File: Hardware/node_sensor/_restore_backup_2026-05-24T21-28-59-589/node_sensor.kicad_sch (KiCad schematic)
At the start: 14 parts, among them J1 Conn_Jack-DC, J2 Pump, J3 Light, U1 DevKitESP32, U2 DHT11, U3 BH1750, U4 ADS1115, U5 DS3231, U6 Soil-Moisture, U7 Soil-Moisture, U8 Soil-Moisture, U9 Soil-Moisture

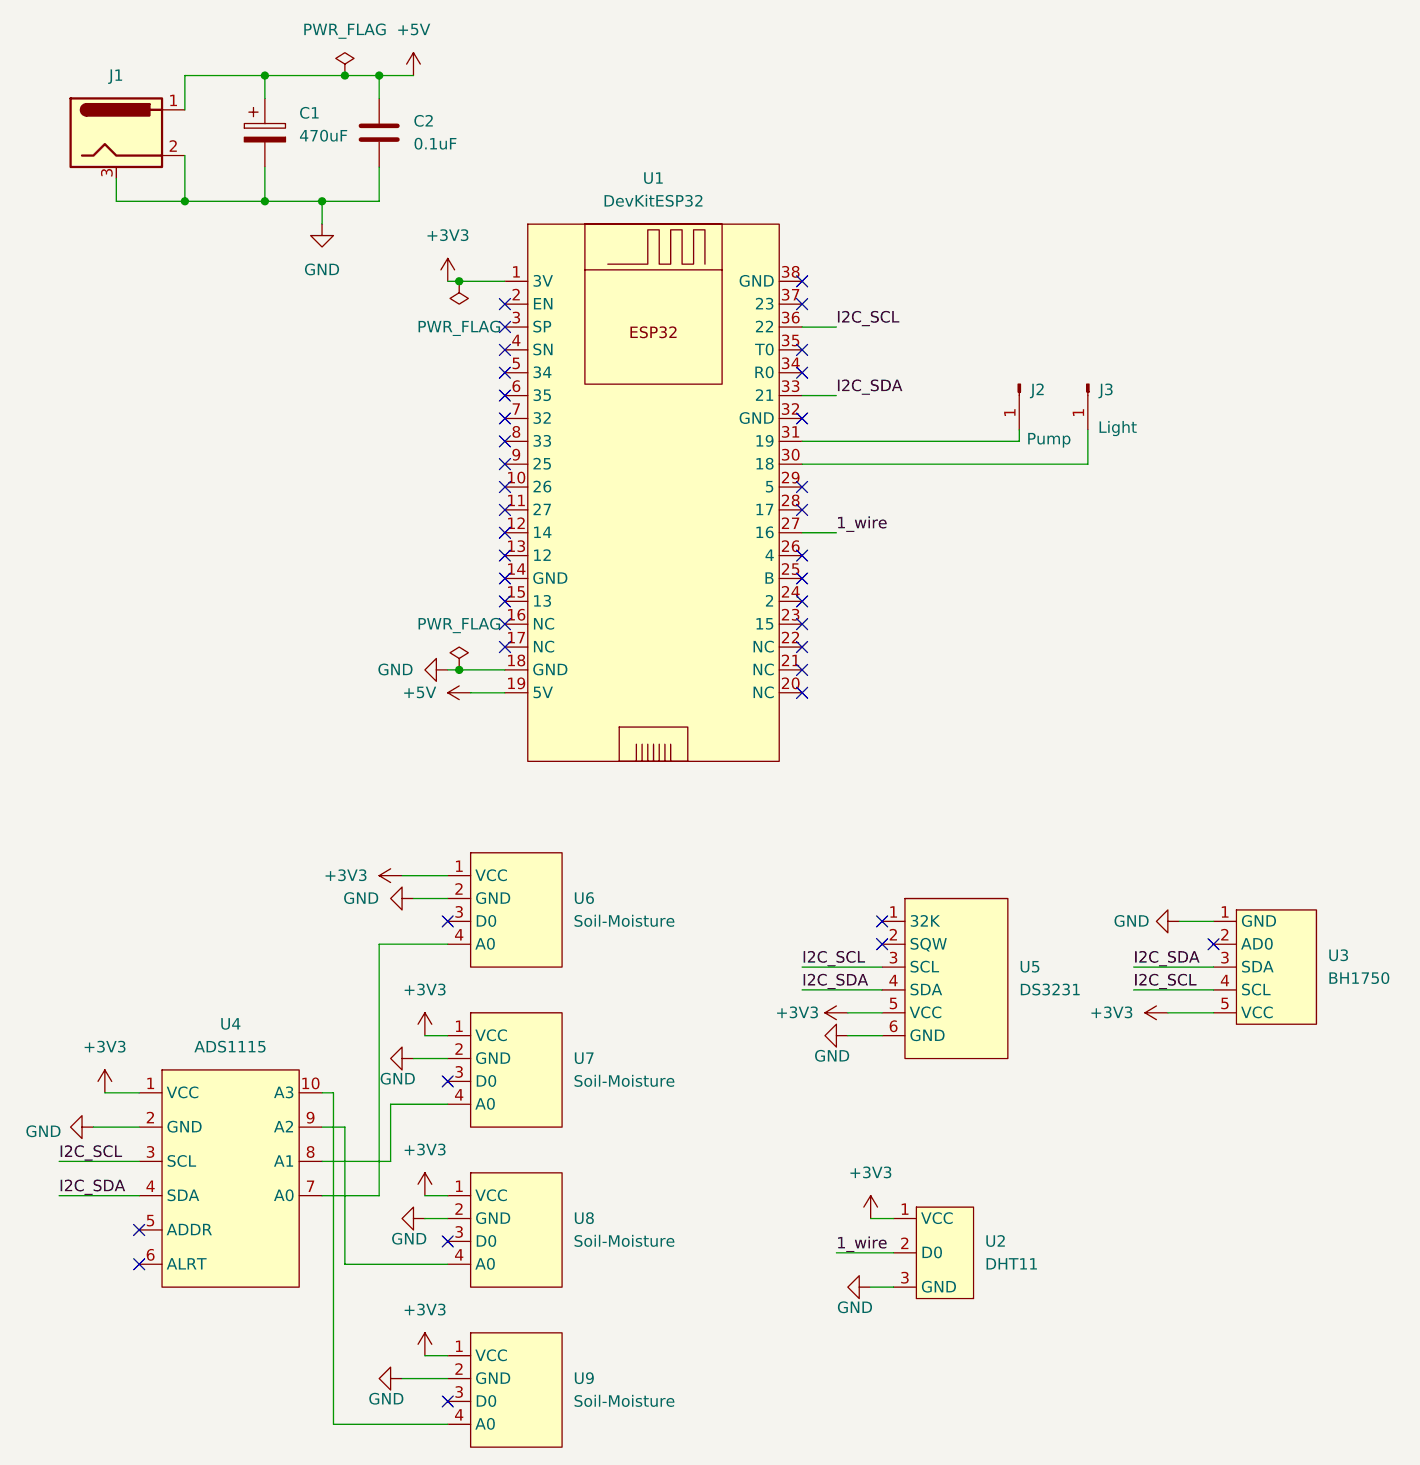
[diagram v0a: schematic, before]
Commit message: updated hardware + fixed conflict Gatway
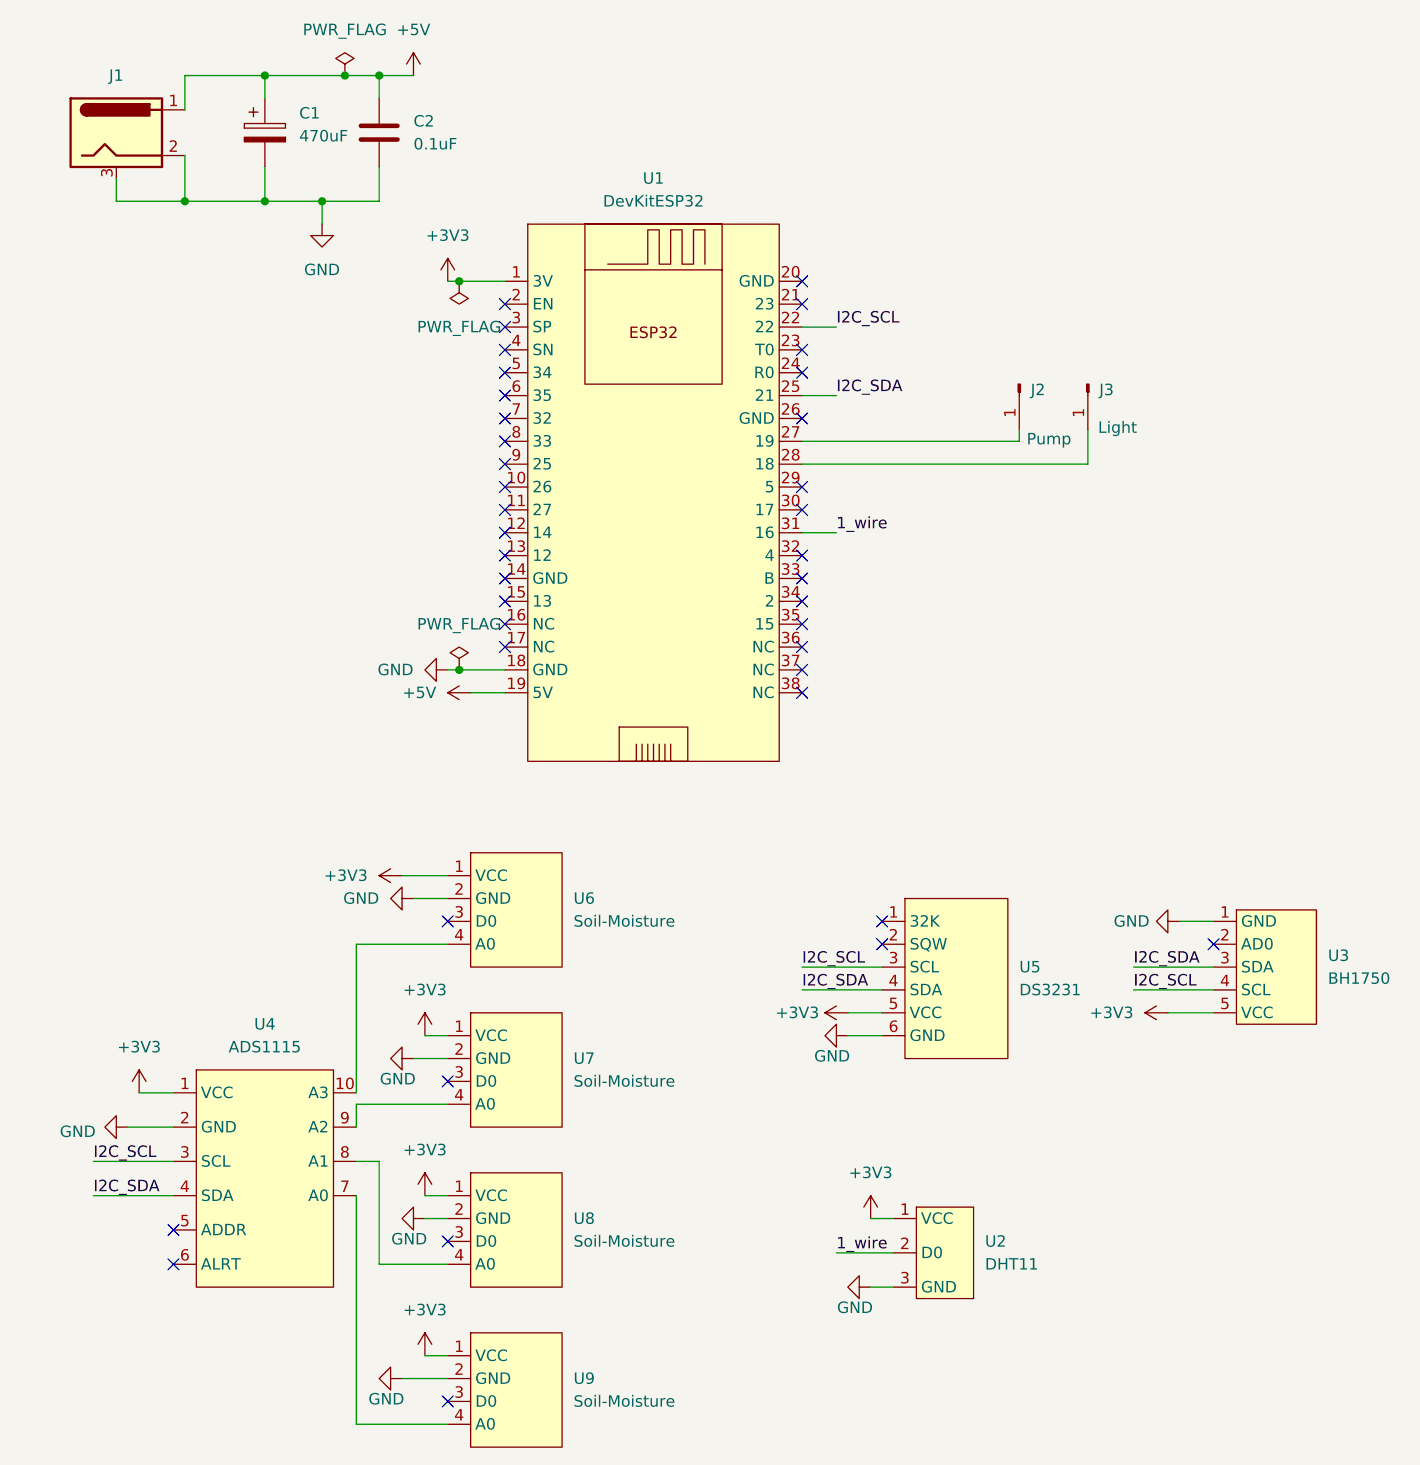
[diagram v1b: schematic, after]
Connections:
- net 1_wire: now also U1.31 (16); no longer U1.27 (16)
- net I2C_SCL: now also U1.22; no longer U1.36 (22)
- net I2C_SDA: now also U1.25 (21); no longer U1.33 (21)
- net at U4.10 (A3): now also U6.4 (A0); no longer U9.4 (A0)
- net at U4.7 (A0): now also U9.4 (A0); no longer U6.4 (A0)
- net at U4.8 (A1): now also U8.4 (A0); no longer U7.4 (A0)
- net at U4.9 (A2): now also U7.4 (A0); no longer U8.4 (A0)
- net at U1.28 (18): now also J3.1 (Pin_1)
- net at U1.30 (17): no longer J3.1 (Pin_1)
- net at J2.1 (Pin_1): now also U1.27 (19); no longer U1.31 (19)
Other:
- moved on the sheet: U4
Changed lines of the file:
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@@
 	)
 	(no_connect
-		(at 25.4 148.59)
+		(at 29.21 148.59)
 	)
 	(no_connect
@@
 	)
 	(no_connect
-		(at 25.4 152.4)
+		(at 29.21 152.4)
 	)
 	(wire
 		(pts
-			(xy 22.86 34.29) (xy 30.48 34.29)
+			(xy 52.07 140.97) (xy 52.07 152.4)
 		)
 		(stroke
@@
 	(wire
 		(pts
-			(xy 59.69 86.36) (xy 60.96 86.36)
+			(xy 22.86 34.29) (xy 30.48 34.29)
 		)
 		(stroke
@@
 	(wire
 		(pts
-			(xy 16.51 144.78) (xy 25.4 144.78)
+			(xy 59.69 86.36) (xy 60.96 86.36)
 		)
 		(stroke
@@
 	(wire
 		(pts
-			(xy 30.48 34.29) (xy 39.37 34.29)
+			(xy 20.32 144.78) (xy 29.21 144.78)
 		)
 		(stroke
@@
 	(wire
 		(pts
-			(xy 54.61 109.22) (xy 59.69 109.22)
+			(xy 30.48 34.29) (xy 39.37 34.29)
 		)
 		(stroke
@@
 	(wire
 		(pts
-			(xy 59.69 43.18) (xy 60.96 43.18)
+			(xy 54.61 109.22) (xy 59.69 109.22)
 		)
 		(stroke
@@
 	(wire
 		(pts
-			(xy 99.06 71.12) (xy 102.87 71.12)
+			(xy 59.69 43.18) (xy 60.96 43.18)
 		)
 		(stroke
@@
 	(wire
 		(pts
-			(xy 60.96 86.36) (xy 66.04 86.36)
+			(xy 99.06 71.12) (xy 102.87 71.12)
 		)
 		(stroke
@@
 	(wire
 		(pts
-			(xy 60.96 43.18) (xy 66.04 43.18)
+			(xy 49.53 137.16) (xy 49.53 134.62)
 		)
 		(stroke
@@
 	(wire
 		(pts
-			(xy 99.06 119.38) (xy 107.95 119.38)
+			(xy 60.96 86.36) (xy 66.04 86.36)
 		)
 		(stroke
@@
 	(wire
 		(pts
-			(xy 48.26 20.32) (xy 52.07 20.32)
+			(xy 49.53 134.62) (xy 59.69 134.62)
 		)
 		(stroke
@@
 	(wire
 		(pts
-			(xy 21.59 133.35) (xy 25.4 133.35)
+			(xy 60.96 43.18) (xy 66.04 43.18)
 		)
 		(stroke
@@
 	(wire
 		(pts
-			(xy 99.06 60.96) (xy 123.19 60.96)
+			(xy 99.06 119.38) (xy 107.95 119.38)
 		)
 		(stroke
@@
 	(wire
 		(pts
-			(xy 57.15 162.56) (xy 59.69 162.56)
+			(xy 48.26 20.32) (xy 52.07 20.32)
 		)
 		(stroke
@@
 	(wire
 		(pts
-			(xy 22.86 31.75) (xy 22.86 34.29)
+			(xy 49.53 133.35) (xy 49.53 116.84)
 		)
 		(stroke
@@
 	(wire
 		(pts
-			(xy 52.07 20.32) (xy 52.07 22.86)
+			(xy 25.4 133.35) (xy 29.21 133.35)
 		)
 		(stroke
@@
 	(wire
 		(pts
-			(xy 59.69 116.84) (xy 52.07 116.84)
+			(xy 99.06 60.96) (xy 123.19 60.96)
 		)
 		(stroke
@@
 	(wire
 		(pts
-			(xy 53.34 140.97) (xy 45.72 140.97)
+			(xy 57.15 162.56) (xy 59.69 162.56)
 		)
 		(stroke
@@
 	(wire
 		(pts
-			(xy 39.37 20.32) (xy 48.26 20.32)
+			(xy 22.86 31.75) (xy 22.86 34.29)
 		)
 		(stroke
@@
 	(wire
 		(pts
-			(xy 53.34 134.62) (xy 53.34 140.97)
+			(xy 52.07 20.32) (xy 52.07 22.86)
 		)
 		(stroke
@@
 	(wire
 		(pts
-			(xy 45.72 34.29) (xy 52.07 34.29)
+			(xy 39.37 20.32) (xy 48.26 20.32)
 		)
 		(stroke
@@
 	(wire
 		(pts
-			(xy 48.26 152.4) (xy 48.26 137.16)
+			(xy 45.72 34.29) (xy 52.07 34.29)
 		)
 		(stroke
@@
 	(wire
 		(pts
-			(xy 46.99 170.18) (xy 46.99 133.35)
-		)
-		(stroke
-			(width 0)
-			(type default)
-		)
-	)
-	(wire
-		(pts
 			(xy 135.89 121.92) (xy 144.78 121.92)
 		)
@@
 	(wire
 		(pts
-			(xy 20.32 137.16) (xy 25.4 137.16)
+			(xy 24.13 137.16) (xy 29.21 137.16)
 		)
 		(stroke
@@
 	(wire
 		(pts
-			(xy 30.48 20.32) (xy 39.37 20.32)
+			(xy 49.53 144.78) (xy 49.53 170.18)
 		)
 		(stroke
@@
 	(wire
 		(pts
-			(xy 130.81 59.69) (xy 130.81 63.5)
+			(xy 30.48 20.32) (xy 39.37 20.32)
 		)
 		(stroke
@@
 	(wire
 		(pts
-			(xy 39.37 30.48) (xy 39.37 34.29)
+			(xy 49.53 116.84) (xy 59.69 116.84)
 		)
 		(stroke
@@
 	(wire
 		(pts
-			(xy 48.26 152.4) (xy 59.69 152.4)
+			(xy 130.81 59.69) (xy 130.81 63.5)
 		)
 		(stroke
@@
 	(wire
 		(pts
-			(xy 99.06 121.92) (xy 107.95 121.92)
+			(xy 39.37 30.48) (xy 39.37 34.29)
 		)
 		(stroke
@@
 	(wire
 		(pts
-			(xy 106.68 147.32) (xy 109.22 147.32)
+			(xy 99.06 121.92) (xy 107.95 121.92)
 		)
 		(stroke
@@
 	(wire
 		(pts
-			(xy 45.72 34.29) (xy 45.72 36.83)
+			(xy 106.68 147.32) (xy 109.22 147.32)
 		)
 		(stroke
@@
 	(wire
 		(pts
-			(xy 54.61 165.1) (xy 59.69 165.1)
+			(xy 45.72 34.29) (xy 45.72 36.83)
 		)
 		(stroke
@@
 	(wire
 		(pts
-			(xy 46.99 170.18) (xy 59.69 170.18)
+			(xy 54.61 165.1) (xy 59.69 165.1)
 		)
 		(stroke
@@
 	(wire
 		(pts
-			(xy 46.99 133.35) (xy 45.72 133.35)
-		)
-		(stroke
-			(width 0)
-			(type default)
-		)
-	)
-	(wire
-		(pts
 			(xy 52.07 20.32) (xy 55.88 20.32)
 		)
@@
 	(wire
 		(pts
-			(xy 48.26 137.16) (xy 45.72 137.16)
-		)
-		(stroke
-			(width 0)
-			(type default)
-		)
-	)
-	(wire
-		(pts
 			(xy 62.23 88.9) (xy 66.04 88.9)
 		)
@@
 	(wire
 		(pts
-			(xy 30.48 20.32) (xy 30.48 24.13)
+			(xy 49.53 170.18) (xy 59.69 170.18)
 		)
 		(stroke
@@
 	(wire
 		(pts
-			(xy 59.69 134.62) (xy 53.34 134.62)
+			(xy 49.53 140.97) (xy 52.07 140.97)
 		)
 		(stroke
@@
 	(wire
 		(pts
-			(xy 16.51 140.97) (xy 25.4 140.97)
+			(xy 30.48 20.32) (xy 30.48 24.13)
 		)
 		(stroke
@@
 	(wire
 		(pts
-			(xy 140.97 114.3) (xy 144.78 114.3)
+			(xy 20.32 140.97) (xy 29.21 140.97)
 		)
 		(stroke
@@
 	(wire
 		(pts
-			(xy 104.14 124.46) (xy 107.95 124.46)
+			(xy 140.97 114.3) (xy 144.78 114.3)
 		)
 		(stroke
@@
 	(wire
 		(pts
-			(xy 52.07 116.84) (xy 52.07 144.78)
+			(xy 52.07 152.4) (xy 59.69 152.4)
 		)
 		(stroke
@@
 	(wire
 		(pts
-			(xy 99.06 55.88) (xy 102.87 55.88)
+			(xy 104.14 124.46) (xy 107.95 124.46)
 		)
 		(stroke
@@
 	(wire
 		(pts
-			(xy 45.72 144.78) (xy 52.07 144.78)
+			(xy 99.06 55.88) (xy 102.87 55.88)
 		)
 		(stroke
@@
 	)
 	(label "I2C_SCL"
-		(at 16.51 140.97 0)
+		(at 20.32 140.97 0)
 		(effects
 			(font
@@
 	)
 	(label "I2C_SDA"
-		(at 16.51 144.78 0)
+		(at 20.32 144.78 0)
 		(effects
 			(font
@@
 	(symbol
 		(lib_id "MY_SYMBOLS:GND")
-		(at 20.32 137.16 270)
+		(at 24.13 137.16 270)
 		(unit 1)
 		(body_style 1)
@@
 		(dnp no)
 		(property "Reference" "#PWR021"
-			(at 13.97 137.16 0)
+			(at 17.78 137.16 0)
 			(hide yes)
 			(show_name no)
@@
 		)
 		(property "Value" "GND"
-			(at 16.764 137.668 90)
+			(at 20.574 137.668 90)
 			(show_name no)
 			(do_not_autoplace no)
@@
 		)
 		(property "Footprint" ""
-			(at 20.32 137.16 0)
+			(at 24.13 137.16 0)
 			(hide yes)
 			(show_name no)
@@
 		)
 		(property "Datasheet" ""
-			(at 20.32 137.16 0)
+			(at 24.13 137.16 0)
 			(hide yes)
 			(show_name no)
@@
 		)
 		(property "Description" "Power symbol creates a global label with name \"GND\" , ground"
-			(at 20.32 137.16 0)
+			(at 24.13 137.16 0)
 			(hide yes)
 			(show_name no)
@@
 	(symbol
 		(lib_id "MY_SYMBOLS:ADS1115-modules")
-		(at 25.4 133.35 0)
+		(at 29.21 133.35 0)
 		(unit 1)
 		(body_style 1)
@@
 		(fields_autoplaced yes)
 		(property "Reference" "U4"
-			(at 35.56 125.73 0)
+			(at 39.37 125.73 0)
 			(show_name no)
 			(do_not_autoplace no)
@@
 		)
 		(property "Value" "ADS1115"
-			(at 35.56 128.27 0)
+			(at 39.37 128.27 0)
 			(show_name no)
 			(do_not_autoplace no)
@@
 		)
 		(property "Footprint" "Connector_PinSocket_2.54mm:PinSocket_1x10_P2.54mm_Vertical"
-			(at 25.4 133.35 0)
+			(at 29.21 133.35 0)
 			(hide yes)
 			(show_name no)
@@
 		)
 		(property "Datasheet" ""
-			(at 25.4 133.35 0)
+			(at 29.21 133.35 0)
 			(hide yes)
 			(show_name no)
@@
 		)
 		(property "Description" ""
-			(at 25.4 133.35 0)
+			(at 29.21 133.35 0)
 			(hide yes)
 			(show_name no)
@@
 	(symbol
 		(lib_id "MY_SYMBOLS:+3V3")
-		(at 21.59 133.35 0)
+		(at 25.4 133.35 0)
 		(unit 1)
 		(body_style 1)
@@
 		(fields_autoplaced yes)
 		(property "Reference" "#PWR020"
-			(at 21.59 137.16 0)
+			(at 25.4 137.16 0)
 			(hide yes)
 			(show_name no)
@@
 		)
 		(property "Value" "+3V3"
-			(at 21.59 128.27 0)
+			(at 25.4 128.27 0)
 			(show_name no)
 			(do_not_autoplace no)
@@
 		)
 		(property "Footprint" ""
-			(at 21.59 133.35 0)
+			(at 25.4 133.35 0)
 			(hide yes)
 			(show_name no)
@@
 		)
 		(property "Datasheet" ""
-			(at 21.59 133.35 0)
+			(at 25.4 133.35 0)
 			(hide yes)
 			(show_name no)
@@
 		)
 		(property "Description" "Power symbol creates a global label with name \"+3V3\""
-			(at 21.59 133.35 0)
+			(at 25.4 133.35 0)
 			(hide yes)
 			(show_name no)
